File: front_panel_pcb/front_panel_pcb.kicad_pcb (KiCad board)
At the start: 2 copper layers, 93.3 x 100 mm, 48 parts, among them SW1 SELECT, SW10 1, SW11 4, SW12 7, SW13 A, SW14 CLEAR, SW15 B, SW16 C, SW17 D, SW18 E, SW2 3, SW3 6, SW4 9, SW5 F, SW6 2, SW7 5, SW8 8, SW9 0

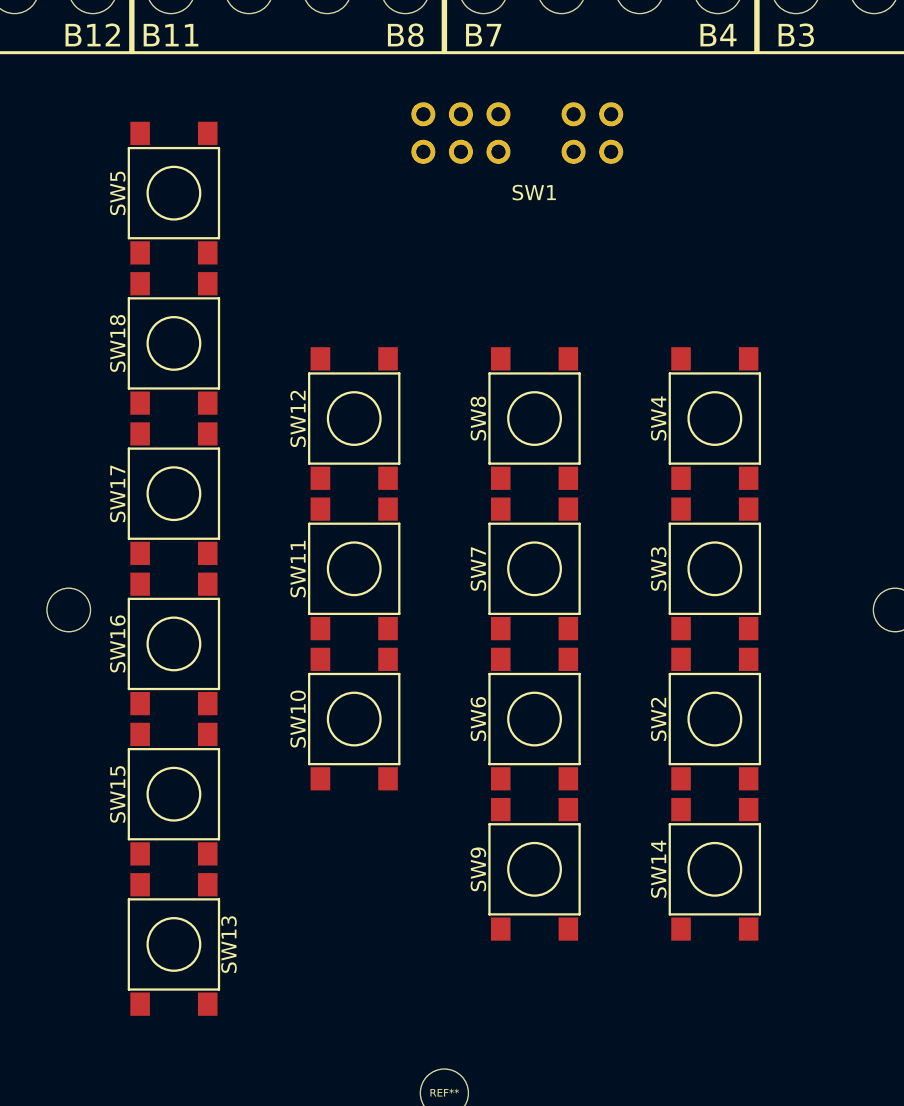
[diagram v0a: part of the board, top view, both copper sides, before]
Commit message: layout front panel keypad with silkscreen
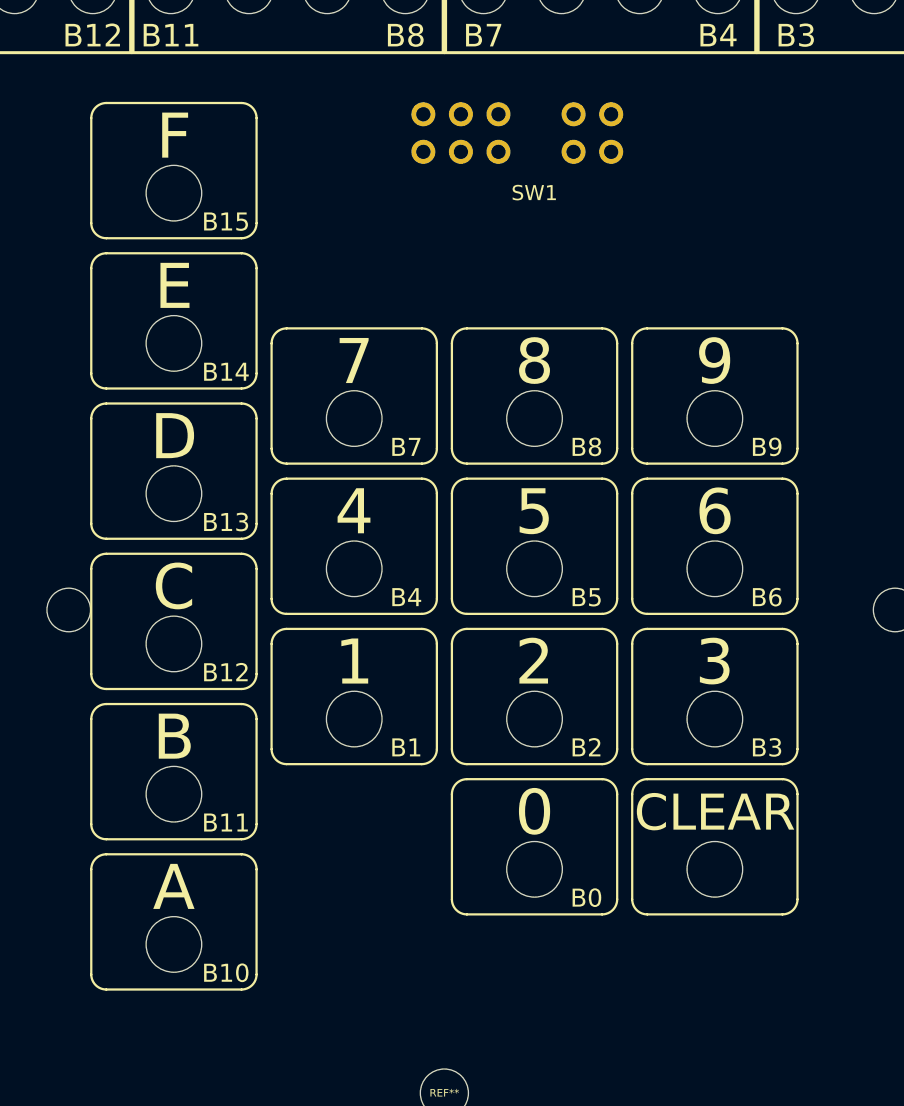
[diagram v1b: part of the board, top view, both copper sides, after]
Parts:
- removed SW10: 1, Switch_CK:CK_PTS645_6mm_SMD
- removed SW11: 4, Switch_CK:CK_PTS645_6mm_SMD
- removed SW12: 7, Switch_CK:CK_PTS645_6mm_SMD
- removed SW13: A, Switch_CK:CK_PTS645_6mm_SMD
- removed SW14: CLEAR, Switch_CK:CK_PTS645_6mm_SMD
- removed SW15: B, Switch_CK:CK_PTS645_6mm_SMD
- removed SW16: C, Switch_CK:CK_PTS645_6mm_SMD
- removed SW17: D, Switch_CK:CK_PTS645_6mm_SMD
- removed SW18: E, Switch_CK:CK_PTS645_6mm_SMD
- removed SW2: 3, Switch_CK:CK_PTS645_6mm_SMD
- removed SW3: 6, Switch_CK:CK_PTS645_6mm_SMD
- removed SW4: 9, Switch_CK:CK_PTS645_6mm_SMD
- removed SW5: F, Switch_CK:CK_PTS645_6mm_SMD
- removed SW6: 2, Switch_CK:CK_PTS645_6mm_SMD
- removed SW7: 5, Switch_CK:CK_PTS645_6mm_SMD
- removed SW8: 8, Switch_CK:CK_PTS645_6mm_SMD
- removed SW9: 0, Switch_CK:CK_PTS645_6mm_SMD
- added REF**: CK_PTS645_FrontPanel, CK_FP:CK_PTS645_FrontPanel, F.Cu at (82.0, 136.8)
- added REF**: CK_PTS645_FrontPanel, CK_FP:CK_PTS645_FrontPanel, F.Cu at (106.0, 121.8)
- added REF**: CK_PTS645_FrontPanel, CK_FP:CK_PTS645_FrontPanel, F.Cu at (118.0, 121.8)
- added REF**: CK_PTS645_FrontPanel, CK_FP:CK_PTS645_FrontPanel, F.Cu at (94.0, 111.8)
- added REF**: CK_PTS645_FrontPanel, CK_FP:CK_PTS645_FrontPanel, F.Cu at (106.0, 111.8)
- added REF**: CK_PTS645_FrontPanel, CK_FP:CK_PTS645_FrontPanel, F.Cu at (118.0, 111.8)
- added REF**: CK_PTS645_FrontPanel, CK_FP:CK_PTS645_FrontPanel, F.Cu at (94.0, 101.8)
- added REF**: CK_PTS645_FrontPanel, CK_FP:CK_PTS645_FrontPanel, F.Cu at (106.0, 101.8)
- added REF**: CK_PTS645_FrontPanel, CK_FP:CK_PTS645_FrontPanel, F.Cu at (82.0, 86.8)
- added REF**: CK_PTS645_FrontPanel, CK_FP:CK_PTS645_FrontPanel, F.Cu at (82.0, 96.8)
- added REF**: CK_PTS645_FrontPanel, CK_FP:CK_PTS645_FrontPanel, F.Cu at (82.0, 106.8)
- added REF**: CK_PTS645_FrontPanel, CK_FP:CK_PTS645_FrontPanel, F.Cu at (118.0, 101.8)
- added REF**: CK_PTS645_FrontPanel, CK_FP:CK_PTS645_FrontPanel, F.Cu at (82.0, 116.8)
- added REF**: CK_PTS645_FrontPanel, CK_FP:CK_PTS645_FrontPanel, F.Cu at (82.0, 126.8)
- added REF**: CK_PTS645_FrontPanel, CK_FP:CK_PTS645_FrontPanel, F.Cu at (106.0, 131.8)
- added REF**: CK_PTS645_FrontPanel, CK_FP:CK_PTS645_FrontPanel, F.Cu at (118.0, 131.8)
- added REF**: CK_PTS645_FrontPanel, CK_FP:CK_PTS645_FrontPanel, F.Cu at (94.0, 121.8)
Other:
- board text added: "0"
- board text added: "1"
- board text added: "2"
- board text added: "3"
- board text added: "4"
- board text added: "5"
- board text added: "6"
- board text added: "7"
- board text added: "8"
- board text added: "9"
- board text added: "A"
- board text added: "B"
- board text added: "B1"
- board text added: "B10"
- board text added: "B13"
- board text added: "B14"
- board text added: "B2"
- board text added: "B5"
- board text added: "B6"
- board text added: "B9"
- board text added: "C"
- board text added: "CLEAR"
- board text added: "D"
- board text added: "E"
- board text added: "F"

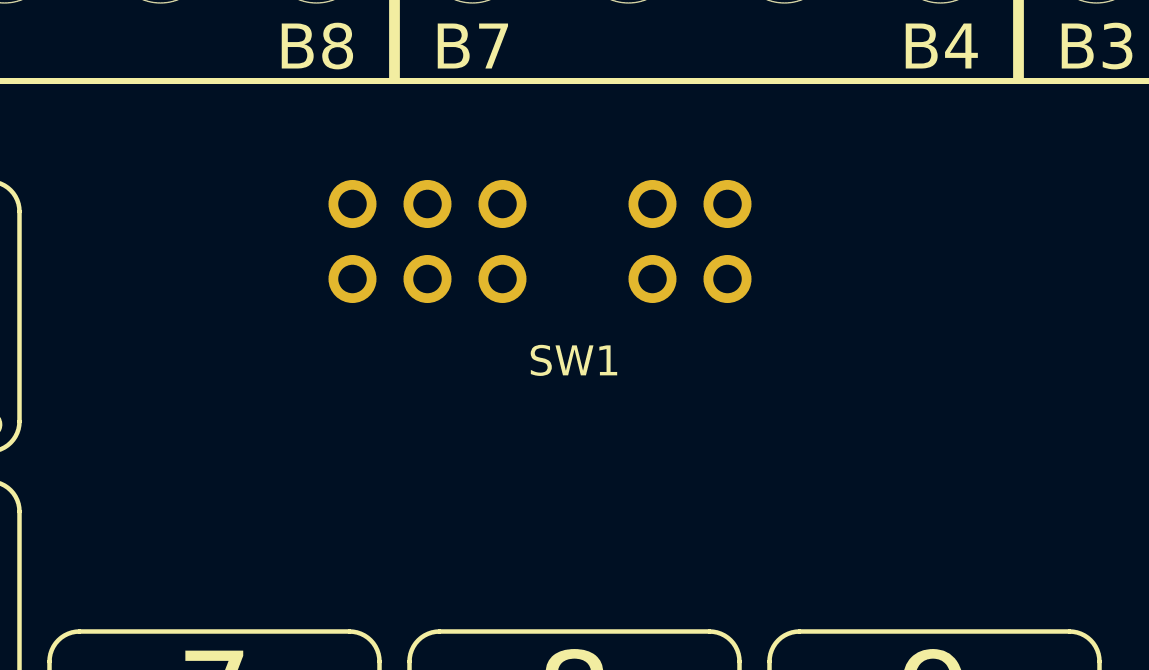
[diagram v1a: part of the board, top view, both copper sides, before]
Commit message: selection switch front panel cutout and silk screen
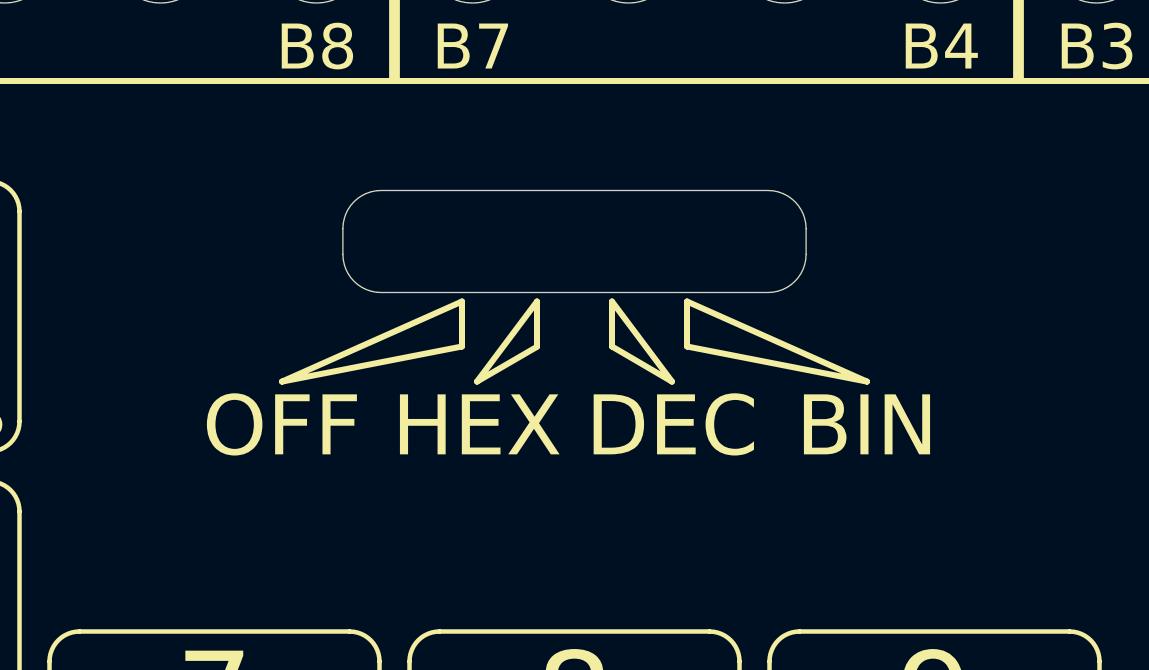
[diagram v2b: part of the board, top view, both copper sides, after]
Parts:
- removed SW1: SELECT, Switch_CK:DP4T_SS-24E06-TG5P
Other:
- outline, holes or cut-outs redrawn
- board text added: "BIN"
- board text added: "CUT OUT"
- board text added: "DEC"
- board text added: "HEX"
- board text added: "OFF"

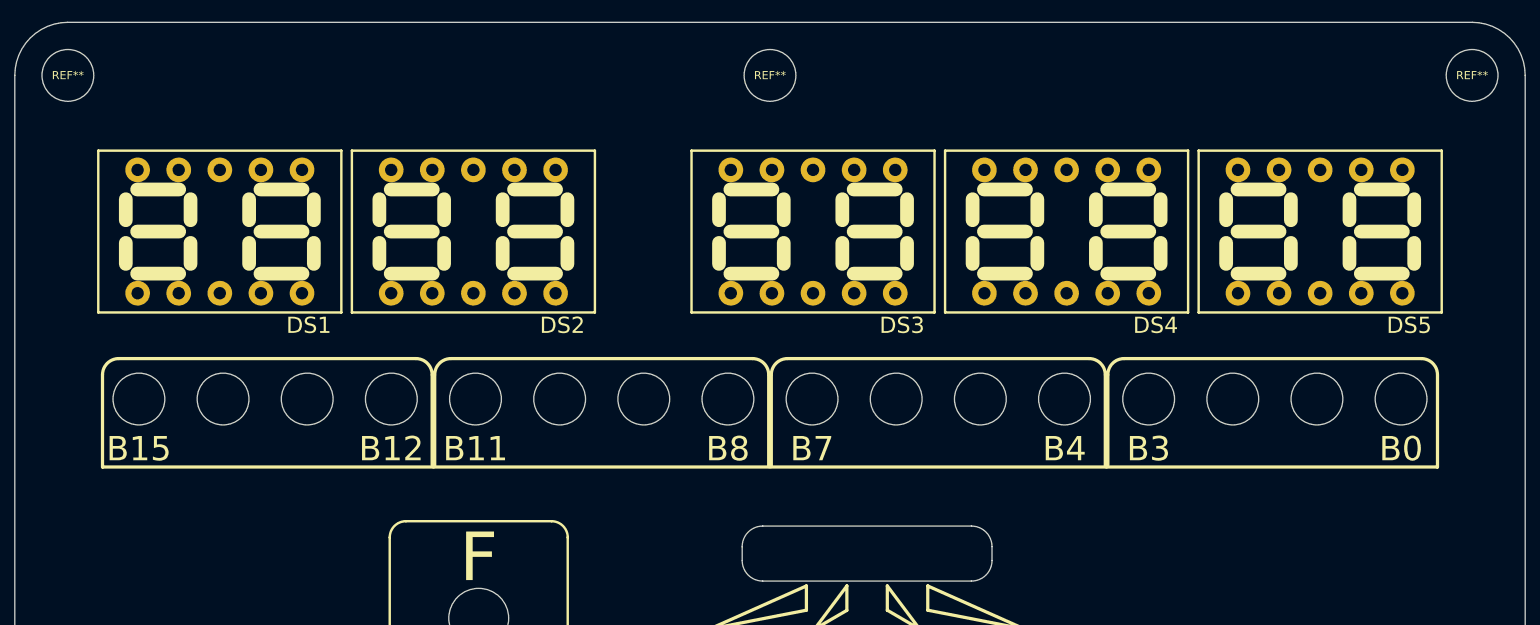
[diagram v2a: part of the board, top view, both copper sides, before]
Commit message: 7seg front panel cutout and silkscreen
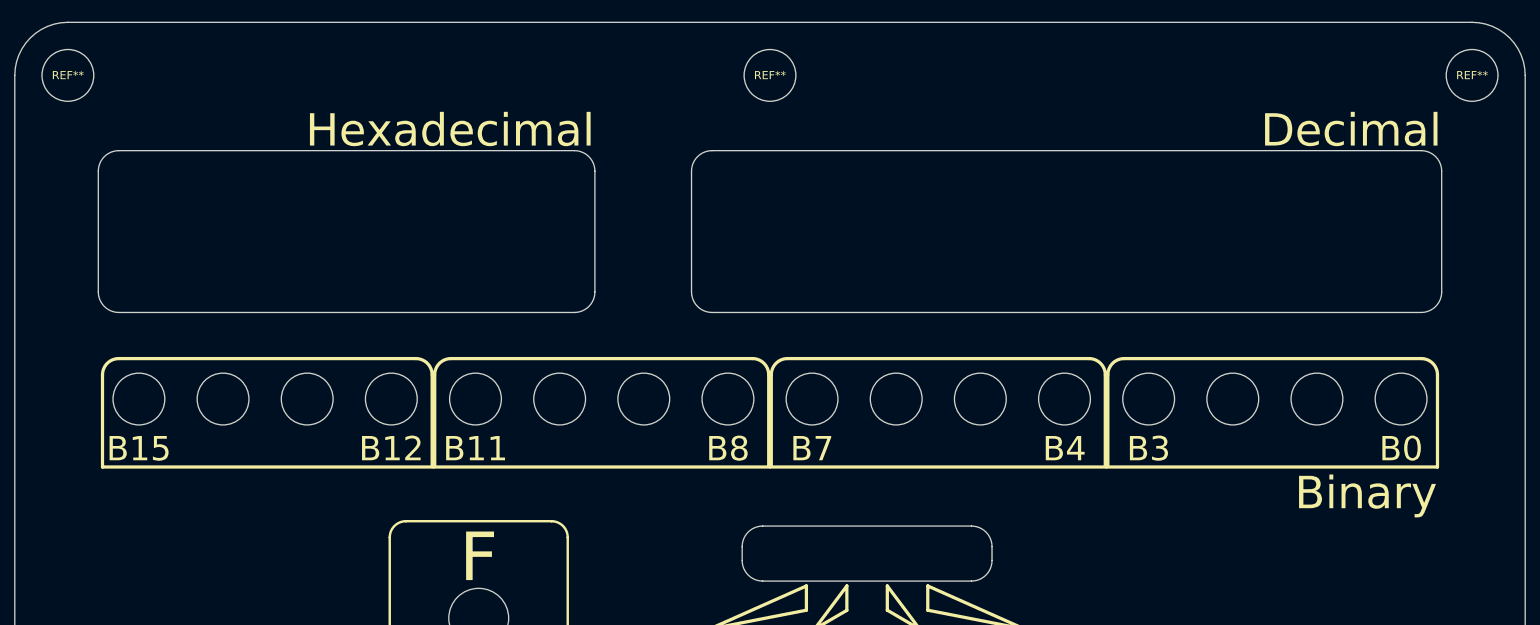
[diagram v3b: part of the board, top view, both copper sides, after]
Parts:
- removed DS1, DS2, DS3, DS4, DS5: LTD-2601WC, Lite-On:Display_Lite-On_LTD-2601WC
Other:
- outline, holes or cut-outs redrawn
- board text added: "Binary"
- board text added: "Decimal"
- board text added: "Hexadecimal"

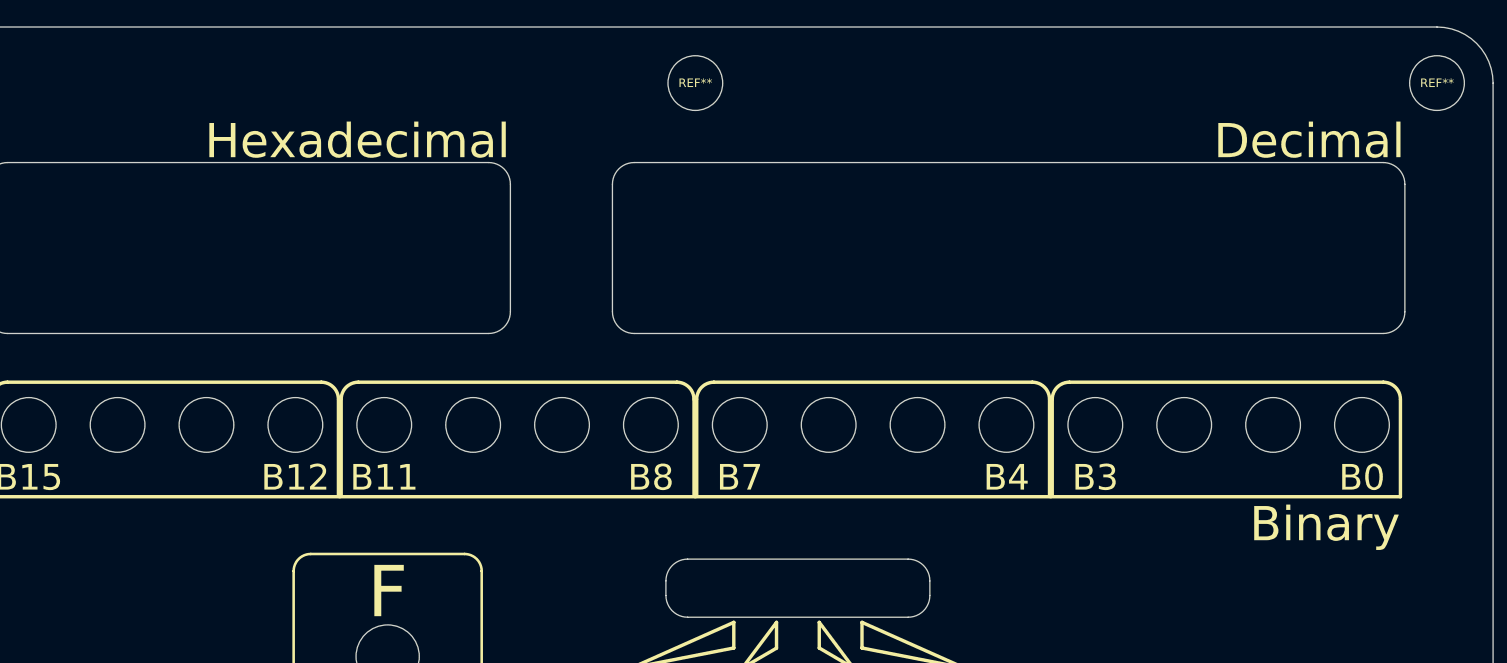
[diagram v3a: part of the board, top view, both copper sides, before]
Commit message: shift lables above 7seg displays left 1.25 and up 0.2
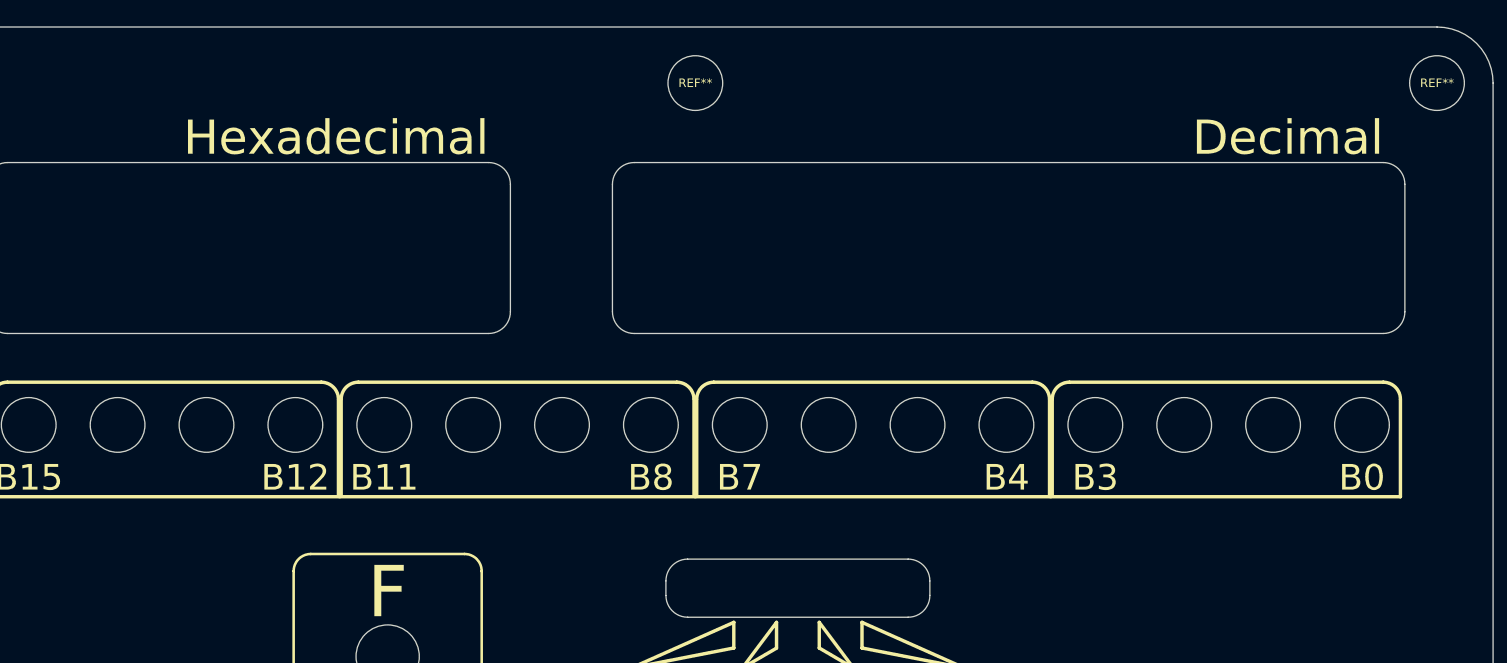
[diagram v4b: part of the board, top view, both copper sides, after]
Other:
- board text removed: "Binary"
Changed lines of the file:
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@@
     (area 53.324999 49.994999 146.675001 150.005001)
     (thickness 1.6)
-    (drawings 117)
+    (drawings 116)
     (tracks 0)
     (zones 0)
@@
     (pad "" np_thru_hole circle (at 0 0) (size 3.7 3.7) (drill 3.7) (layers *.Cu *.Mask))
   )
-  (gr_text Binary (at 141.24 79.1) (layer F.SilkS)
+  (gr_text Decimal (at 140.26 56.49) (layer F.SilkS)
     (effects (font (size 2 2) (thickness 0.35)) (justify right))
   )
-  (gr_text Decimal (at 141.51 56.69) (layer F.SilkS)
+  (gr_text Hexadecimal (at 87.92 56.49) (layer F.SilkS)
     (effects (font (size 2 2) (thickness 0.35)) (justify right))
   )
-  (gr_text Hexadecimal (at 89.17 56.69) (layer F.SilkS)
-    (effects (font (size 2 2) (thickness 0.35)) (justify right))
-  )
